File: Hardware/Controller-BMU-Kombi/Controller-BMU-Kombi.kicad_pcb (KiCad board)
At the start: 2 copper layers, 129.5 x 109.2 mm, 45 parts, among them J1 Conn_01x05_Socket, J10 Conn_01x03_Pin, J11 Conn_01x03_Pin, J12 Conn_01x03_Pin, J13 Conn_01x03_Pin, J14 Conn_01x03_Pin, J15 Conn_01x03_Pin, J16 Conn_01x03_Pin, J17 Conn_01x03_Pin, J18 Conn_01x03_Pin, J19 Conn_01x03_Pin, J2 Conn_01x05_Socket, J20 Conn_01x03_Pin, J21 Conn_01x03_Pin, J22 Conn_01x03_Pin, J23 Conn_01x03_Pin, J24 Conn_01x03_Pin, J25 Conn_01x03_Socket, J26 Conn_01x04_Socket, J3 Conn_01x05_Socket, J4 Conn_01x05_Socket, J5 Conn_01x05_Socket, J6 Conn_01x05_Socket, J7 Conn_01x03_Pin, J8 Conn_01x03_Pin, J9 Conn_01x03_Pin, U2 ESP32_NODEMCU, U9 PCA9555PW

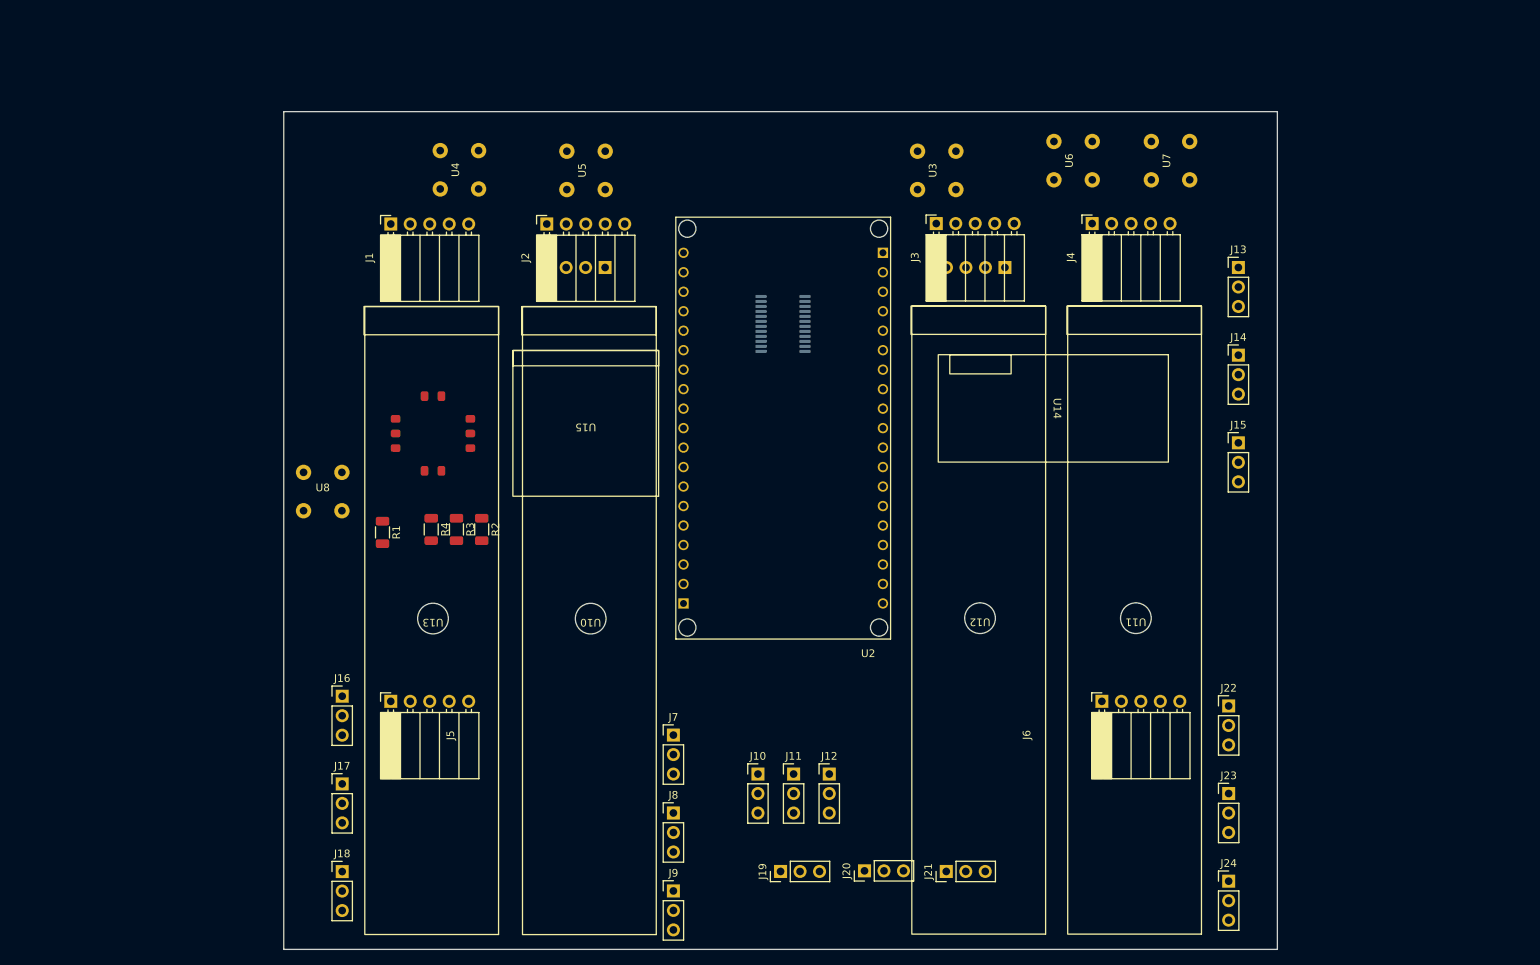
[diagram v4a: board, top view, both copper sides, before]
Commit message: Finished Controller-BMU-Kombi PCB
routing finished + finishing touches applied
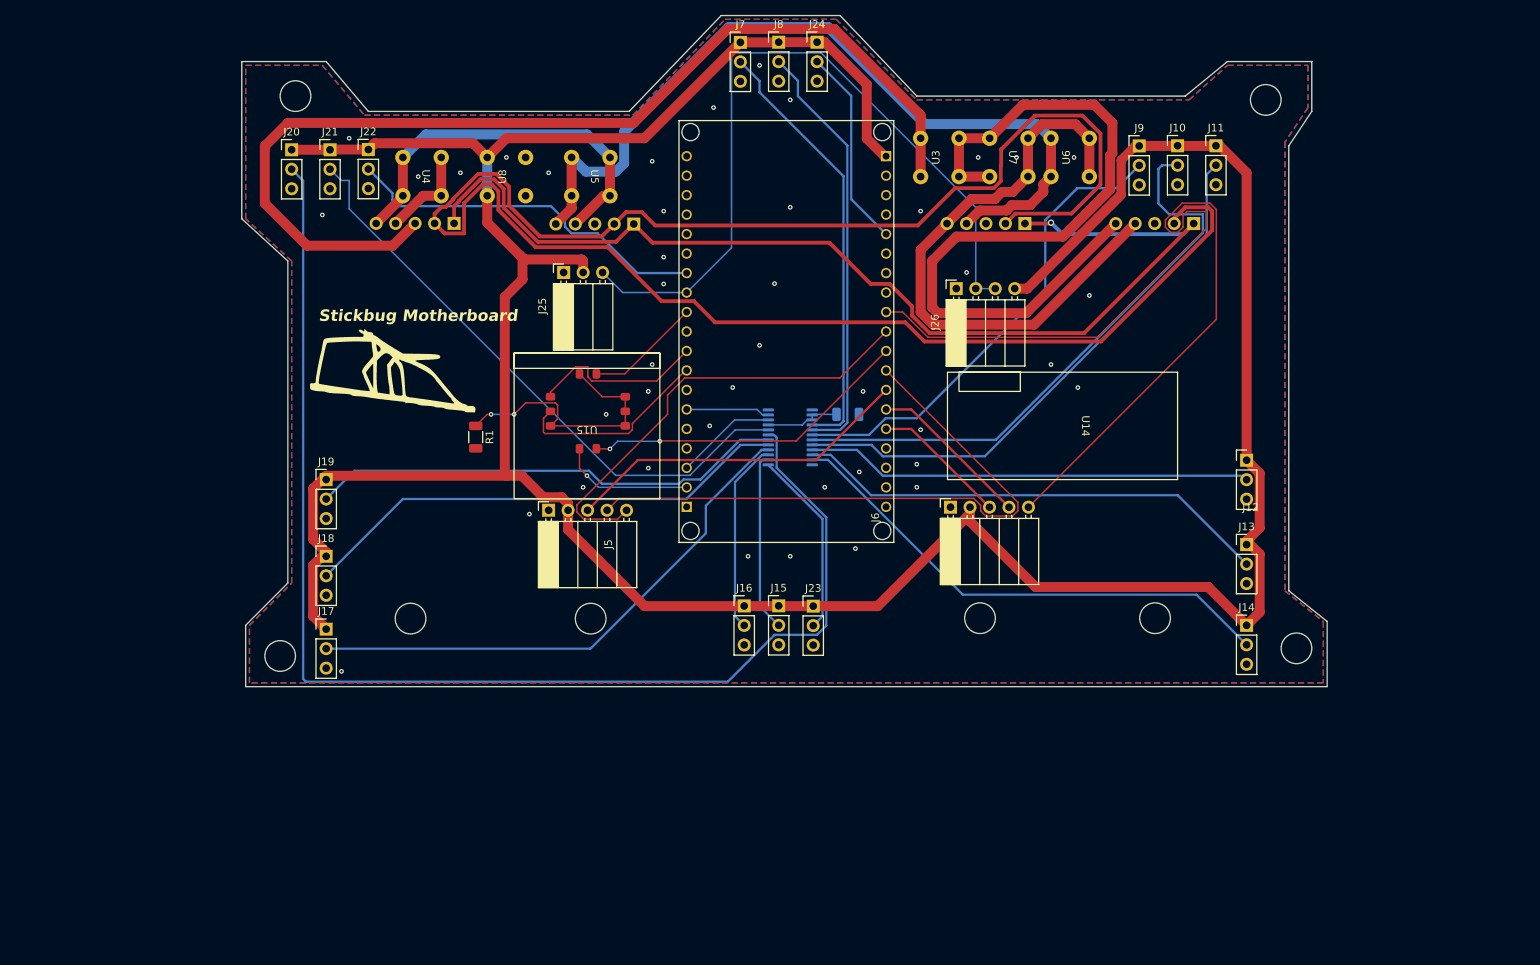
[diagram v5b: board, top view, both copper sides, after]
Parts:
- removed R3, R4: 10k, Resistor_SMD:R_1206_3216Metric
- J1, J2, J3, J4, R2, U10, U11, U12, U13: moved to B.Cu
- J25, J26: moved to F.Cu
- moved J22 133.6 mm to (88.5, 54.5)
- moved J21 123.7 mm to (83.5, 54.5), turned to 0 degrees
- moved J24 121.8 mm to (147.0, 40.5)
- moved J20 120.1 mm to (78.5, 54.5), turned to 0 degrees
- moved J9 114.6 mm to (189.0, 54.0)
- moved J8 101.4 mm to (142.0, 40.5)
- moved J11 98.7 mm to (199.0, 54.0)
- moved J10 98.5 mm to (194.0, 54.0)
- moved J7 90.7 mm to (137.0, 40.5)
- moved J19 78.2 mm to (83.0, 97.5), turned to 0 degrees
- moved J12 68.1 mm to (203.0, 95.0)
- moved J15 63.6 mm to (142.0, 114.0)
- moved J23 59.4 mm to (146.5, 114.0)
- moved J16 53.7 mm to (137.5, 114.0)
- moved R2 50.0 mm to (151.0, 89.0), turned to 0 degrees
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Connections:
- U2 pad J5_10: SW2 -> SW1
- U9 pad 2: Net-(U9-A1) -> Net-(U9-A0)
- U9 pad 3: Net-(U9-A2) -> Net-(U9-A0)
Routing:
- net +5V: track 0.00 -> 418.6 mm
- net Net-(J1-Pin_2): track 0.00 -> 259.2 mm
- net SERV15: track 0.00 -> 166.9 mm
- net Net-(J1-Pin_1): track 0.00 -> 141.7 mm, vias 0 -> 1
- net Net-(J1-Pin_3): track 0.00 -> 135.0 mm
- net SW2: track 0.00 -> 116.7 mm
- net CELL3+: track 0.00 -> 108.2 mm
- net CELL4-: track 0.00 -> 102.8 mm
- net DATA: track 0.00 -> 98.9 mm
- net VRY1: track 0.00 -> 81.3 mm
- net CELL4+: track 0.00 -> 79.7 mm
- net SERV16: track 0.00 -> 78.3 mm
- net SERV4: track 0.00 -> 78.1 mm
- net SERV5: track 0.00 -> 73.5 mm
- net SERV12: track 0.00 -> 70.5 mm
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- added copper zone on B.Cu, net GND
- added copper zone on F.Cu, net GND
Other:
- board size 129.5 x 109.2 mm -> 141.5 x 87.5 mm
- board text added: "Stickbug Motherboard"

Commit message: final updates
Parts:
- J25: value Conn_01x03_Socket -> Conn_01x05_Socket; footprint Connector_PinSocket_2.54mm:PinSocket_1x03_P2.54mm_Horizontal -> Connector_PinSocket_2.54mm:PinSocket_1x05_P2.54mm_Horizontal
- J26: value Conn_01x04_Socket -> Conn_01x05_Socket; footprint Connector_PinSocket_2.54mm:PinSocket_1x04_P2.54mm_Horizontal -> Connector_PinSocket_2.54mm:PinSocket_1x05_P2.54mm_Horizontal
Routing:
- net CELL4-: track 102.8 -> 105.4 mm
- net CELL4+: track 79.7 -> 82.3 mm
- net Net-(J1-Pin_2): track 259.2 -> 261.3 mm
- net +5V: track 418.6 -> 419.9 mm
- net GND: vias 42 -> 46
